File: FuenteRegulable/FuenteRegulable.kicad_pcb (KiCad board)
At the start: 2 copper layers, 3 parts, among them J1 AC_IN, J2 T_IN, J3 T_OUT

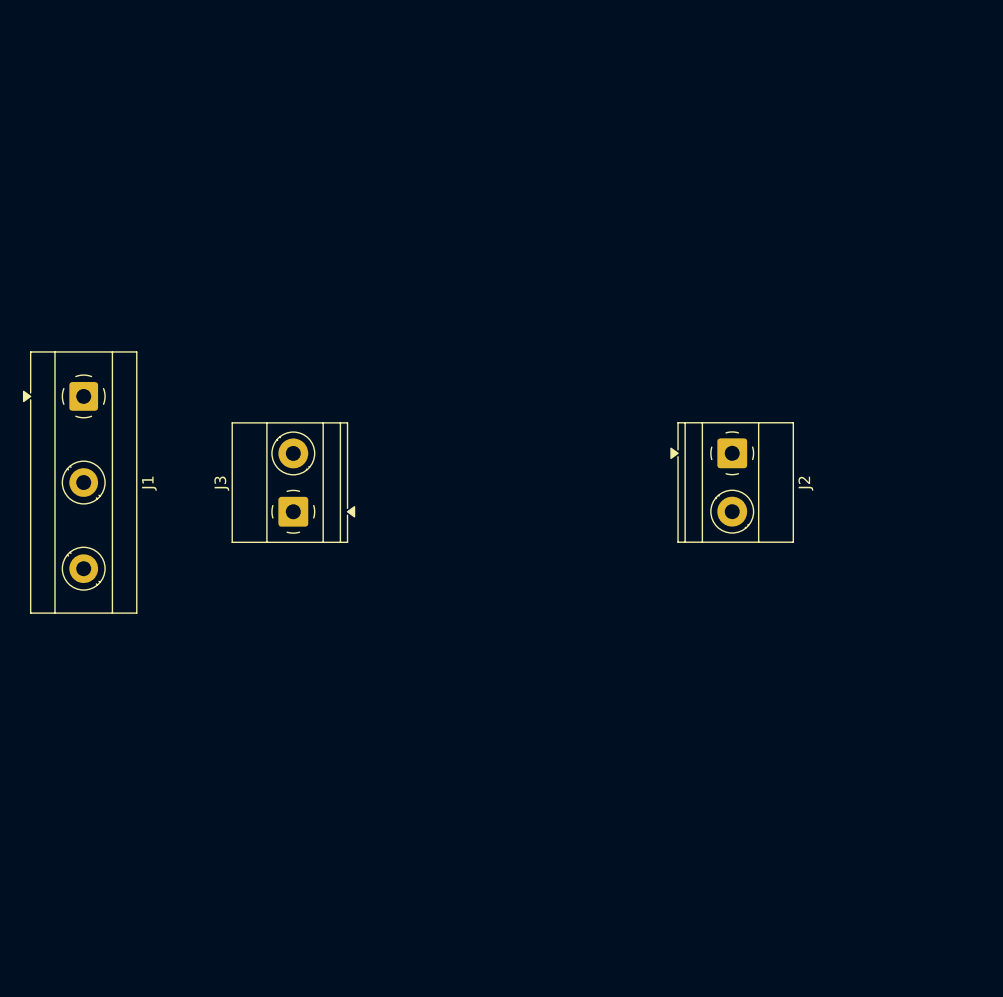
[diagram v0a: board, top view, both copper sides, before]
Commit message: Diagrama esquematico terminado
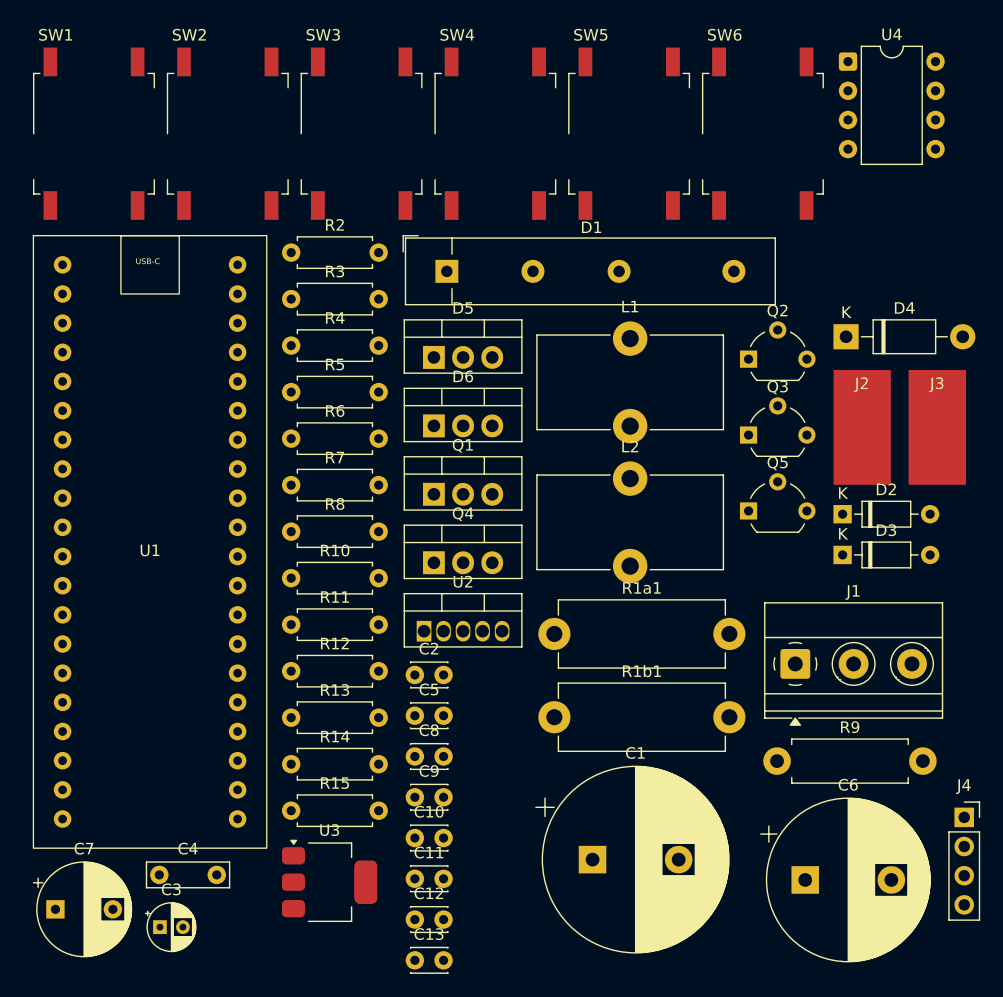
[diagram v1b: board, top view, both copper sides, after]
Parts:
- added C1: 2200uF/35V, Capacitor_THT:CP_Radial_D16.0mm_P7.50mm, F.Cu at (153.1, 124.1)
- added C10: 100nF, Capacitor_THT:C_Disc_D3.0mm_W2.0mm_P2.50mm, F.Cu at (137.7, 122.2)
- added C11: 100nF, Capacitor_THT:C_Disc_D3.0mm_W2.0mm_P2.50mm, F.Cu at (137.7, 125.7)
- added C12: 100nF, Capacitor_THT:C_Disc_D3.0mm_W2.0mm_P2.50mm, F.Cu at (137.7, 129.3)
- added C13: 100nF, Capacitor_THT:C_Disc_D3.0mm_W2.0mm_P2.50mm, F.Cu at (137.7, 132.8)
- added C2: 8,2nF, Capacitor_THT:C_Disc_D3.0mm_W2.0mm_P2.50mm, F.Cu at (137.7, 108.0)
- added C3: 10uF, Capacitor_THT:CP_Radial_D4.0mm_P2.00mm, F.Cu at (115.5, 129.9)
- added C4: 4,7nF, Capacitor_THT:C_Rect_L7.0mm_W2.0mm_P5.00mm, F.Cu at (115.4, 125.4)
- added C5: 100nF, Capacitor_THT:C_Disc_D3.0mm_W2.0mm_P2.50mm, F.Cu at (137.7, 111.5)
- added C6: 1000uF/35V, Capacitor_THT:CP_Radial_D14.0mm_P7.50mm, F.Cu at (171.7, 125.8)
- added C7: 100uF/16V, Capacitor_THT:CP_Radial_D8.0mm_P5.00mm, F.Cu at (106.4, 128.4)
- added C8: 100nF, Capacitor_THT:C_Disc_D3.0mm_W2.0mm_P2.50mm, F.Cu at (137.7, 115.1)
- added C9: 100nF, Capacitor_THT:C_Disc_D3.0mm_W2.0mm_P2.50mm, F.Cu at (137.7, 118.6)
- added D1: GBP206, Diode_THT:Diode_Bridge_32.0x5.6x17.0mm_P10.0mm_P7.5mm, F.Cu at (140.4, 72.8)
- added D2: 1N4148, Diode_THT:D_DO-35_SOD27_P7.62mm_Horizontal, F.Cu at (174.9, 94.0)
- added D3: 1N4148, Diode_THT:D_DO-35_SOD27_P7.62mm_Horizontal, F.Cu at (174.9, 97.5)
- added D4: 10V, Diode_THT:D_DO-41_SOD81_P10.16mm_Horizontal, F.Cu at (175.2, 78.5)
- added D5: MBR20100, Package_TO_SOT_THT:TO-220-3_Vertical, F.Cu at (139.3, 80.3)
- added D6: MBR20100, Package_TO_SOT_THT:TO-220-3_Vertical, F.Cu at (139.3, 86.3)
- added J4: OLED_I2C, Connector_PinSocket_2.54mm:PinSocket_1x04_P2.54mm_Vertical, F.Cu at (185.5, 120.4)
- added L1: 10mHy, Inductor_THT:L_Toroid_Vertical_L16.0mm_W8.0mm_P7.62mm, F.Cu at (156.4, 78.7)
- added L2: 150uHy, Inductor_THT:L_Toroid_Vertical_L16.0mm_W8.0mm_P7.62mm, F.Cu at (156.4, 90.9)
- added Q1: IRF540N, Package_TO_SOT_THT:TO-220-3_Vertical, F.Cu at (139.3, 92.2)
- added Q2: 2N3904, Package_TO_SOT_THT:TO-92_Wide, F.Cu at (166.7, 80.5)
- added Q3: 2N7000, Package_TO_SOT_THT:TO-92_Wide, F.Cu at (166.7, 87.1)
- added Q4: IRF540N, Package_TO_SOT_THT:TO-220-3_Vertical, F.Cu at (139.3, 98.2)
- added Q5: 2N3904, Package_TO_SOT_THT:TO-92_Wide, F.Cu at (166.7, 93.7)
- added R10: ??, Resistor_THT:R_Axial_DIN0207_L6.3mm_D2.5mm_P7.62mm_Horizontal, F.Cu at (126.9, 99.5)
- added R11: ??, Resistor_THT:R_Axial_DIN0207_L6.3mm_D2.5mm_P7.62mm_Horizontal, F.Cu at (126.9, 103.6)
- added R12: ??, Resistor_THT:R_Axial_DIN0207_L6.3mm_D2.5mm_P7.62mm_Horizontal, F.Cu at (126.9, 107.7)
- added R13: ??, Resistor_THT:R_Axial_DIN0207_L6.3mm_D2.5mm_P7.62mm_Horizontal, F.Cu at (126.9, 111.7)
- added R14: ??, Resistor_THT:R_Axial_DIN0207_L6.3mm_D2.5mm_P7.62mm_Horizontal, F.Cu at (126.9, 115.8)
- added R15: ??, Resistor_THT:R_Axial_DIN0207_L6.3mm_D2.5mm_P7.62mm_Horizontal, F.Cu at (126.9, 119.8)
- added R1a1: 150R/2W, Resistor_THT:R_Axial_DIN0614_L14.3mm_D5.7mm_P15.24mm_Horizontal, F.Cu at (149.8, 104.4)
- added R1b1: 150R/2W, Resistor_THT:R_Axial_DIN0614_L14.3mm_D5.7mm_P15.24mm_Horizontal, F.Cu at (149.8, 111.7)
- added R2: 3K3, Resistor_THT:R_Axial_DIN0207_L6.3mm_D2.5mm_P7.62mm_Horizontal, F.Cu at (126.9, 71.2)
- added R3: 5K6, Resistor_THT:R_Axial_DIN0207_L6.3mm_D2.5mm_P7.62mm_Horizontal, F.Cu at (126.9, 75.2)
- added R4: 10K, Resistor_THT:R_Axial_DIN0207_L6.3mm_D2.5mm_P7.62mm_Horizontal, F.Cu at (126.9, 79.3)
- added R5: 8K2, Resistor_THT:R_Axial_DIN0207_L6.3mm_D2.5mm_P7.62mm_Horizontal, F.Cu at (126.9, 83.3)
- added R6: 6K8, Resistor_THT:R_Axial_DIN0207_L6.3mm_D2.5mm_P7.62mm_Horizontal, F.Cu at (126.9, 87.4)
- added R7: 10K, Resistor_THT:R_Axial_DIN0207_L6.3mm_D2.5mm_P7.62mm_Horizontal, F.Cu at (126.9, 91.5)
- added R8: 11K, Resistor_THT:R_Axial_DIN0207_L6.3mm_D2.5mm_P7.62mm_Horizontal, F.Cu at (126.9, 95.5)
- added R9: 0R1 / 0.5W, Resistor_THT:R_Axial_DIN0411_L9.9mm_D3.6mm_P12.70mm_Horizontal, F.Cu at (169.2, 115.5)
- added SW1: SW_MEC_5E, Button_Switch_SMD:SW_MEC_5GSH9, F.Cu at (109.7, 60.9)
- added SW2: SW_MEC_5E, Button_Switch_SMD:SW_MEC_5GSH9, F.Cu at (121.4, 60.9)
- added SW3: SW_MEC_5E, Button_Switch_SMD:SW_MEC_5GSH9, F.Cu at (133.0, 60.9)
- added SW4: SW_MEC_5E, Button_Switch_SMD:SW_MEC_5GSH9, F.Cu at (144.7, 60.9)
- added SW5: SW_MEC_5E, Button_Switch_SMD:SW_MEC_5GSH9, F.Cu at (156.3, 60.9)
- added SW6: SW_MEC_5E, Button_Switch_SMD:SW_MEC_5GSH9, F.Cu at (168.0, 60.9)
- added U1: ~, STM32:STM32BlackPill, F.Cu at (114.6, 97.7)
- added U2: LM2576T-5, Package_TO_SOT_THT:TO-220-5_Vertical, F.Cu at (138.5, 104.2)
- added U3: AMS1117-3.3, Package_TO_SOT_SMD:SOT-223-3_TabPin2, F.Cu at (130.2, 126.0)
- added U4: TL082, Package_DIP:DIP-8_W7.62mm, F.Cu at (175.4, 54.6)
- J1: footprint TerminalBlock_MetzConnect:TerminalBlock_MetzConnect_Type171_RT13703HBWC_1x03_P7.50mm_Horizontal -> TerminalBlock_Phoenix:TerminalBlock_Phoenix_MKDS-1,5-3-5.08_1x03_P5.08mm_Horizontal
- J2: value T_IN -> OUT-P; footprint TerminalBlock_Phoenix:TerminalBlock_Phoenix_MKDS-1,5-2-5.08_1x02_P5.08mm_Horizontal -> Connector_Wire:SolderWirePad_1x01_SMD_5x10mm
- J3: value T_OUT -> OUT-N; footprint TerminalBlock_Phoenix:TerminalBlock_Phoenix_MKDS-1,5-2-5.08_1x02_P5.08mm_Horizontal -> Connector_Wire:SolderWirePad_1x01_SMD_5x10mm
- moved J1 66.2 mm to (170.8, 107.0), turned to 0 degrees
- moved J3 56.6 mm to (183.2, 86.4), turned to 0 degrees
- moved J2 11.5 mm to (176.6, 86.4), turned to 0 degrees
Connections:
- J1 pad 1: Earth -> /AC_N
- J1 pad 2: 220VAC_N -> Earth
- J1 pad 3: 220VAC_L -> /AC_L
- J2 pad 1: 220VAC_L -> Io_ADC
- J3 pad 1: unconnected-(J3-Pin_1-Pad1) -> Load_N

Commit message: Comienzo a rutear PCB
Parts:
- D5, D6: footprint Package_TO_SOT_THT:TO-220-3_Vertical -> Package_TO_SOT_THT:TO-220-3_Horizontal_TabDown
- J4, SW1, SW2, SW3, SW4, SW5, SW6: moved to B.Cu
- moved C6 104.1 mm to (99.4, 50.9), turned to -90 degrees
- moved SW6 102.9 mm to (85.3, 122.1), turned to 180 degrees
- moved J1 102.8 mm to (76.2, 66.7), turned to -90 degrees
- moved SW2 102.8 mm to (194.4, 133.2), turned to 180 degrees
- moved C4 99.5 mm to (193.6, 63.8), turned to -90 degrees
- moved SW3 98.4 mm to (210.1, 122.1), turned to 180 degrees
- moved SW1 98.4 mm to (194.4, 111.0), turned to 180 degrees
- moved C3 95.4 mm to (188.7, 68.8), turned to 90 degrees
- moved R6 87.0 mm to (205.7, 50.7), turned to -90 degrees
- moved R7 84.5 mm to (205.7, 61.2), turned to -90 degrees
- moved R8 82.1 mm to (201.4, 61.2), turned to -90 degrees
- moved R4 79.5 mm to (202.6, 54.8), turned to 180 degrees
- moved R12 79.5 mm to (206.3, 111.4)
- moved C1 77.2 mm to (99.4, 68.7), turned to -90 degrees
- moved SW5 76.1 mm to (111.2, 122.1), turned to 180 degrees
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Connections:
- J4 pad 1: +3V3 -> GND
- J4 pad 2: GND -> +3V3
- J4 pad 3: I2C_SDA -> I2C_SCL
- J4 pad 4: I2C_SCL -> I2C_SDA
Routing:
- net /Vs: track 0.00 -> 189.5 mm
- net +5V: track 0.00 -> 141.9 mm
- net Io_MeasP: track 0.00 -> 110.5 mm
- net Load_N: track 0.00 -> 109.6 mm
- net Net-(D3-A): track 0.00 -> 74.1 mm
- net BTN_RETURN: track 0.00 -> 72.6 mm
- net BTN_PLUS: track 0.00 -> 62.1 mm
- net GND: track 0.00 -> 60.9 mm
- net SHUTDOWN: track 0.00 -> 51.6 mm
- net BTN_DOWN: track 0.00 -> 49.6 mm
- net BTN_ENTER: track 0.00 -> 47.6 mm
- net Net-(D6-K): track 0.00 -> 46.1 mm
- net Io_ADC: track 0.00 -> 45.7 mm
- net Net-(D3-K): track 0.00 -> 43.6 mm
- net Net-(D4-K): track 0.00 -> 40.7 mm
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- added copper zone on B.Cu, net GND
- added copper zone on F.Cu, net GND
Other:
- board outline added: 150 x 100 mm

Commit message: PCB Terminado
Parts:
- J2, J3: moved to B.Cu
- moved J3 30.1 mm to (217.8, 56.7)
- moved J2 29.9 mm to (217.8, 86.7)
- moved C1 4.00 mm to (103.4, 68.7)
- moved C6 4.00 mm to (103.4, 50.9)
- moved D1 4.00 mm to (90.6, 50.9)
- moved J1 4.00 mm to (80.2, 66.7)
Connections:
- U1 pad 1: BTN_MINUS -> BTN_RETURN
- U1 pad 11: BTN_DOWN -> BTN_UP
- U1 pad 12: BTN_RETURN -> BTN_PLUS
- U1 pad 2: BTN_UP -> BTN_ENTER
- U1 pad 3: BTN_PLUS -> BTN_MINUS
- U1 pad 4: BTN_ENTER -> BTN_DOWN
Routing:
- net +3V3: track 24.3 -> 319.5 mm
- net I2C_SCL: track 0.00 -> 64.6 mm
- net GND: track 60.9 -> 0.00 mm
- net I2C_SDA: track 0.00 -> 58.5 mm
- net Io_ADC: track 45.7 -> 81.7 mm
- net BTN_MINUS: track 29.5 -> 60.1 mm
- net BTN_DOWN: track 49.6 -> 79.3 mm
- net BTN_ENTER: track 47.6 -> 70.2 mm
- net BTN_RETURN: track 72.6 -> 93.3 mm
- net BTN_UP: track 35.9 -> 50.6 mm
- net Load_N: track 109.6 -> 122.4 mm
- net BTN_PLUS: track 62.1 -> 72.7 mm
- net SHUTDOWN: track 51.6 -> 57.4 mm
- net /Vs: track 189.5 -> 192.3 mm
- net +5V: track 141.9 -> 143.6 mm
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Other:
- outline, holes or cut-outs redrawn
